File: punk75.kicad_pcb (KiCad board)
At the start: 2 copper layers, 285.8 x 124.6 mm, 184 parts, among them J1 AVR-ISP-6, SW1 RESET, SW2 BOOT, U1 ATmega32A-PU, Y1 16MHz

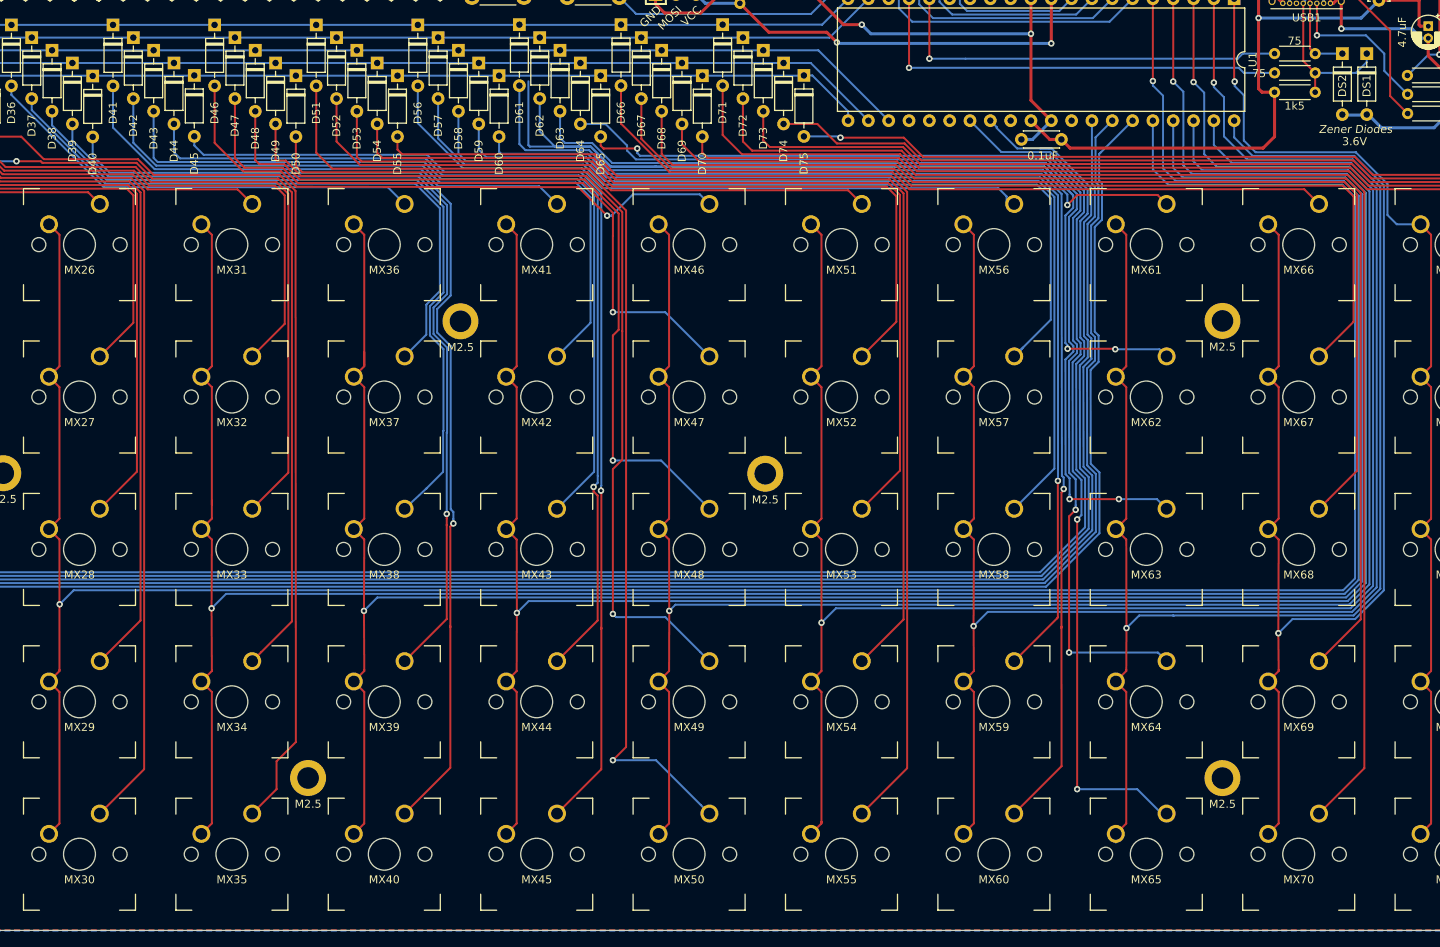
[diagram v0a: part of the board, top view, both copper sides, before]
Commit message: added extra switches to allow 2u in bottom row
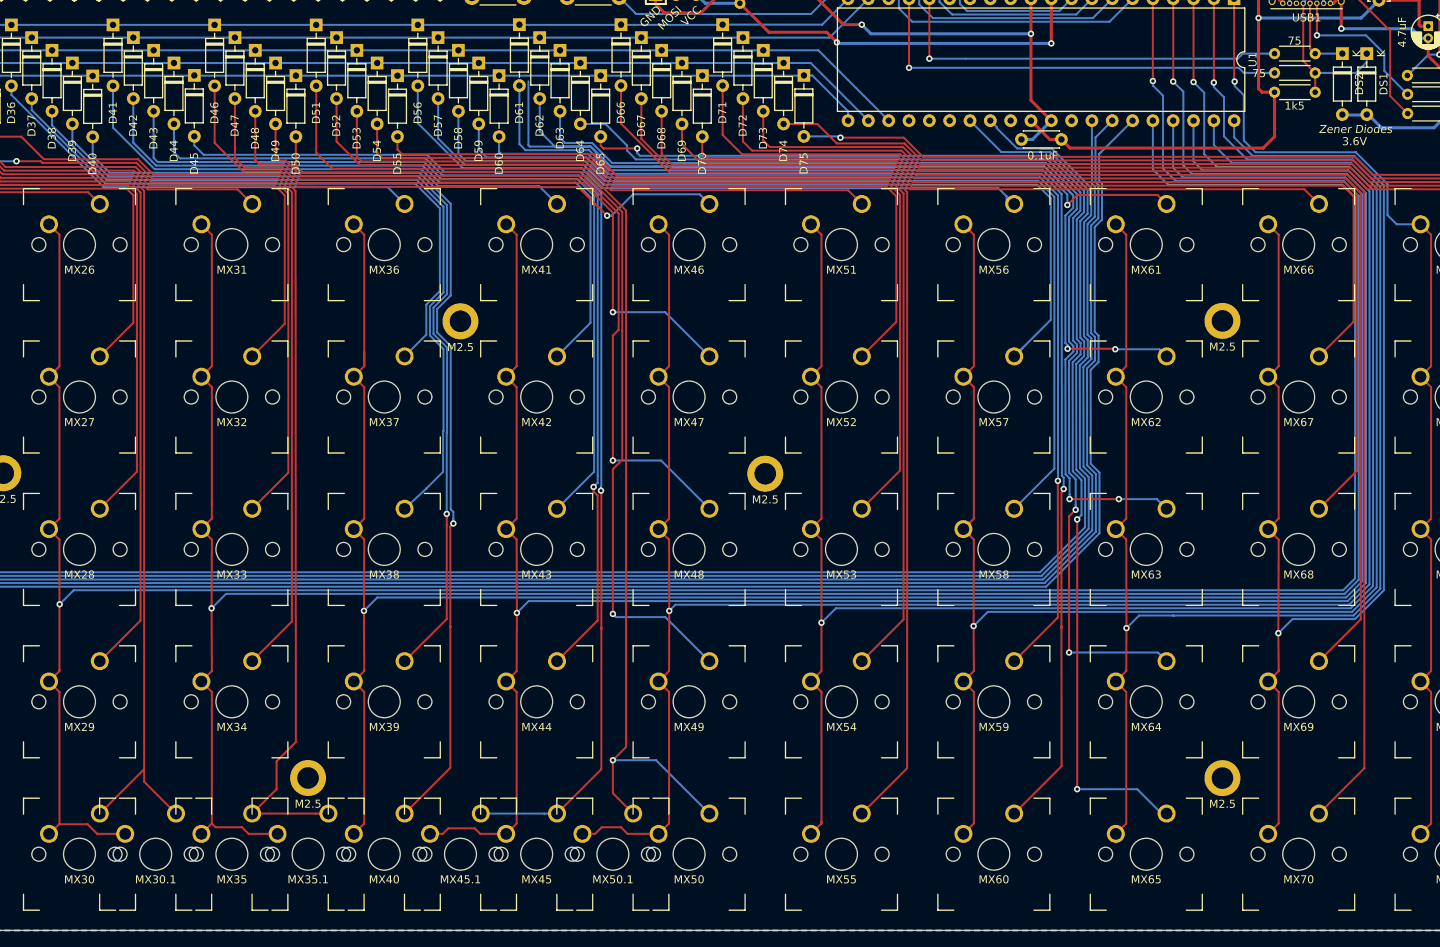
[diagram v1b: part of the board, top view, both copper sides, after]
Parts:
- added MX30.1: MX-NoLED, modded_footprints:MXOnly-1U-NoLED, F.Cu at (193.7, 220.7)
- added MX35.1: MX-NoLED, modded_footprints:MXOnly-1U-NoLED, F.Cu at (212.7, 220.7)
- added MX45.1: MX-NoLED, modded_footprints:MXOnly-1U-NoLED, F.Cu at (231.8, 220.7)
- added MX50.1: MX-NoLED, modded_footprints:MXOnly-1U-NoLED, F.Cu at (250.8, 220.7)
- DS1, DS2: footprint modded_footprints:D_DO-35_SOD27_P7.62mm_Horizontal -> Diode_THT:D_DO-35_SOD27_P7.62mm_Horizontal
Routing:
- net COL9: track 247.2 -> 257.4 mm
- net COL8: track 282.6 -> 292.7 mm
- net Net-(D35-Pad2): track 121.0 -> 130.5 mm
- net Net-(D45-Pad2): track 135.1 -> 144.1 mm
- net COL5: track 324.3 -> 333.0 mm
- net COL6: track 321.5 -> 330.2 mm
- net Net-(D50-Pad2): track 131.5 -> 139.2 mm
- net Net-(D30-Pad2): track 115.8 -> 123.0 mm

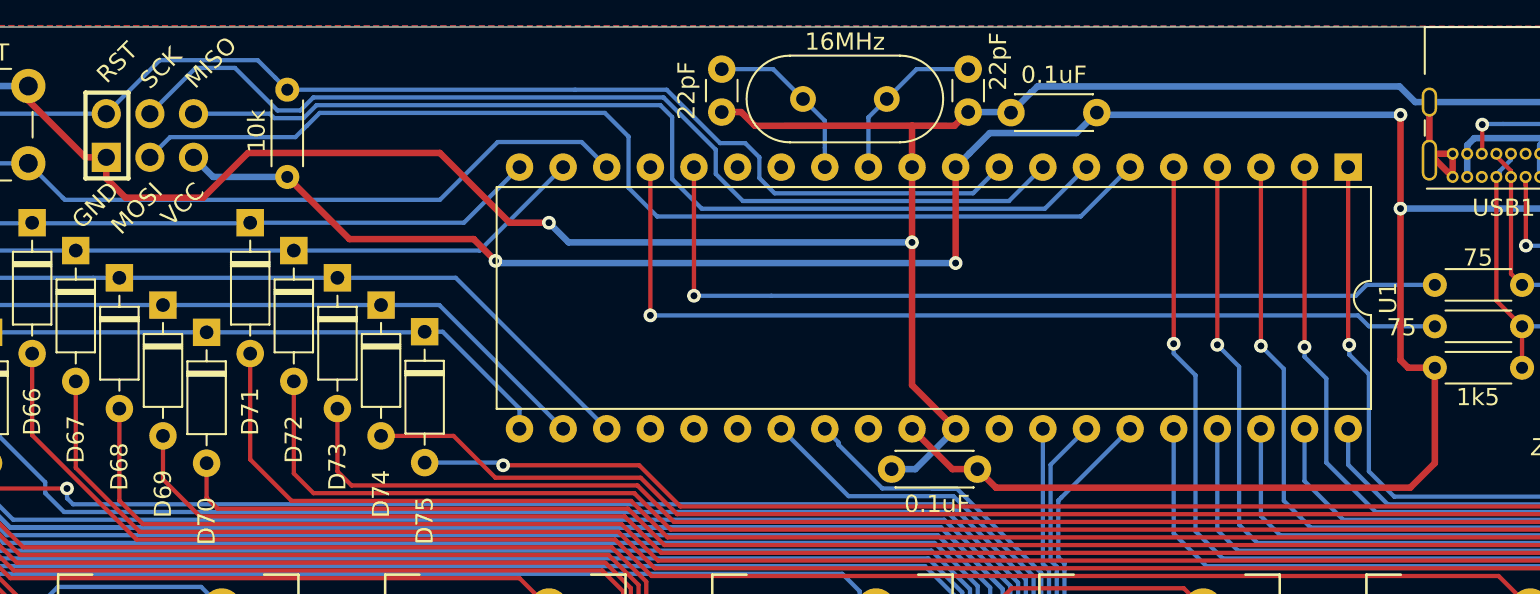
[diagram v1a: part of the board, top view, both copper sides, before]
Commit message: changed usb tracks using differential pair
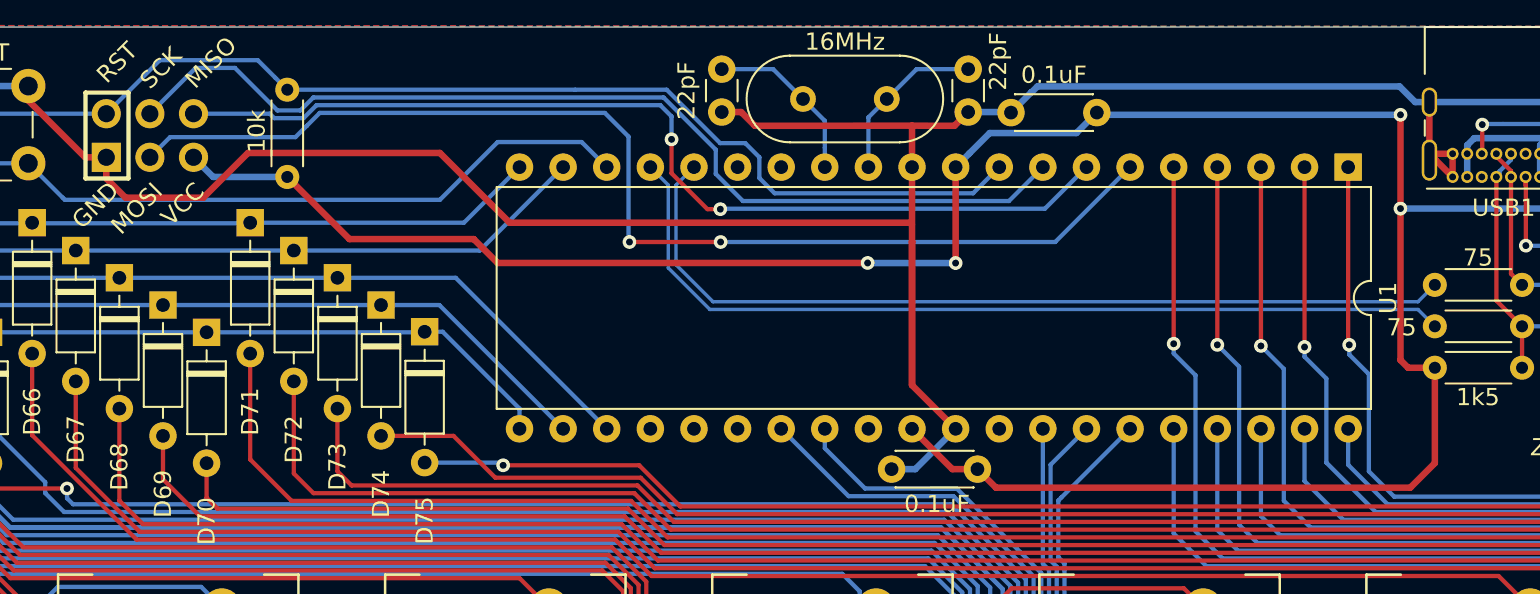
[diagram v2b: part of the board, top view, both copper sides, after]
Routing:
- net GND: track 208.8 -> 216.7 mm, vias 3 -> 1
- net MOSI: track 63.6 -> 66.6 mm, vias 0 -> 2
- net D-: track 55.1 -> 52.9 mm, vias 1 -> 0
- net D+: track 51.5 -> 52.2 mm, vias 1 -> 0
- net COL1: track 350.1 -> 350.7 mm
- net MISO: track 58.0 -> 57.9 mm, vias 0 -> 2

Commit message: added extra decoration
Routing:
- added copper zone on B.Cu, net (none)
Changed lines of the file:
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@@
     (36 B.SilkS user)
     (37 F.SilkS user)
-    (38 B.Mask user hide)
-    (39 F.Mask user hide)
+    (38 B.Mask user)
+    (39 F.Mask user)
     (40 Dwgs.User user hide)
     (41 Cmts.User user hide)
@@
       )
     )
+  )
+  (zone (net 0) (net_name "") (layer B.Cu) (hatch edge 0.508)
+    (connect_pads (clearance 0.508))
+    (min_thickness 0.254)
+    (fill yes (arc_segments 32) (thermal_gap 0.508) (thermal_bridge_width 0.508))
+    (polygon
+      (pts
+        (xy 334.01 165.862) (xy 331.47 170.307) (xy 326.263 170.307) (xy 323.723 165.862) (xy 326.263 161.29)
+        (xy 331.47 161.29)
+      )
+    )
+  )
+  (zone (net 0) (net_name "") (layer B.Cu) (hatch edge 0.508)
+    (connect_pads (clearance 0.508))
+    (min_thickness 0.254)
+    (fill yes (arc_segments 32) (thermal_gap 0.508) (thermal_bridge_width 0.508))
+    (polygon
+      (pts
+        (xy 325.501 170.688) (xy 322.961 175.26) (xy 317.754 175.26) (xy 315.087 170.688) (xy 317.754 166.243)
+        (xy 322.961 166.243)
+      )
+    )
+  )
+  (zone (net 0) (net_name "") (layer B.Cu) (hatch edge 0.508)
+    (connect_pads (clearance 0.508))
+    (min_thickness 0.254)
+    (fill yes (arc_segments 32) (thermal_gap 0.508) (thermal_bridge_width 0.508))
+    (polygon
+      (pts
+        (xy 334.01 175.768) (xy 331.47 180.213) (xy 326.263 180.213) (xy 323.596 175.768) (xy 326.263 171.196)
+        (xy 331.47 171.196)
+      )
+    )

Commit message: changed footprints to my modded MX-Alps hybrids
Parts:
- MX1, MX10, MX11, MX12, MX13, MX14, MX15, MX16, MX17, MX18, MX19, MX2, MX20, MX21, MX22, MX23, MX24, MX25, MX26, MX27, MX28, MX29, MX3, MX30, MX31, MX32, MX33, MX34, MX35, MX36, MX37, MX38, MX39, MX4, MX40, MX41, MX42, MX43, MX44, MX45, MX46, MX47, MX48, MX49, MX5, MX50, MX51, MX52, MX53, MX54, MX55, MX56, MX57, MX58, MX59, MX6, MX60, MX61, MX62, MX63, MX64, MX65, MX66, MX67, MX68, MX69, MX7, MX70, MX71, MX72, MX73, MX74, MX75, MX8, MX9: footprint modded_footprints:MXOnly-1U-NoLED -> MX_Alps_Hybrid:MX-1U-NoLED
- MX30.1, MX35.1, MX45.1, MX50.1: footprint modded_footprints:MXOnly-1U-NoLED -> MX_Alps_Hybrid:MX-2U-NoLED
- turned MX30.1 to 180 degrees
- turned MX35.1 to 180 degrees
- turned MX45.1 to 180 degrees
- turned MX50.1 to 180 degrees
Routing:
- net COL6: track 330.2 -> 345.6 mm
- net COL5: track 333.0 -> 346.2 mm
- net Net-(D30-Pad2): track 123.0 -> 135.1 mm, vias 0 -> 1
- net Net-(D45-Pad2): track 144.1 -> 153.8 mm
- net COL8: track 292.7 -> 301.2 mm
- net Net-(D50-Pad2): track 139.2 -> 147.7 mm
- net Net-(D35-Pad2): track 130.5 -> 137.8 mm
- net COL7: track 287.7 -> 292.4 mm
- net Net-(D40-Pad2): track 130.0 -> 131.8 mm
- net COL9: track 257.4 -> 256.6 mm

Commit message: added configurable led and rewired all colums to new ports
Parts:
- added LED2: LED2, LED_THT:LED_D3.0mm, F.Cu at (351.9, 111.5)
- added R8: 1k5, Resistor_THT:R_Axial_DIN0204_L3.6mm_D1.6mm_P5.08mm_Horizontal, F.Cu at (350.1, 121.2)
- moved LED1 2.86 mm to (357.0, 111.5)
- moved C5 0.95 mm to (352.7, 116.2)
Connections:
- U1 pad 1: COL14 -> Net-(U1-Pad1)
- U1 pad 15: Net-(U1-Pad15) -> LED2
- U1 pad 2: COL12 -> Net-(U1-Pad2)
- U1 pad 24: Net-(U1-Pad24) -> COL0
- U1 pad 25: Net-(U1-Pad25) -> COL1
- U1 pad 26: Net-(U1-Pad26) -> COL4
- U1 pad 27: COL0 -> COL3
- U1 pad 28: COL1 -> COL2
- U1 pad 3: COL10 -> COL13
- U1 pad 33: COL2 -> COL5
- U1 pad 34: COL3 -> COL6
- U1 pad 35: COL4 -> COL7
- U1 pad 36: COL5 -> COL8
- U1 pad 37: COL7 -> COL10
- U1 pad 38: COL9 -> COL12
- U1 pad 39: COL11 -> COL14
- U1 pad 4: COL8 -> COL11
- U1 pad 40: COL13 -> Net-(U1-Pad40)
- U1 pad 5: COL6 -> COL9
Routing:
- net LED2: track 0.00 -> 64.3 mm, vias 0 -> 4
- net COL13: track 169.9 -> 190.8 mm, vias 1 -> 2
- net COL4: track 288.1 -> 308.5 mm
- net COL11: track 208.4 -> 228.0 mm, vias 1 -> 2
- net COL9: track 256.6 -> 274.3 mm, vias 1 -> 2
- net COL3: track 305.5 -> 321.7 mm
- net COL8: track 301.2 -> 286.6 mm, vias 2 -> 1
- net COL10: track 244.2 -> 230.9 mm, vias 2 -> 1
- net COL6: track 345.6 -> 332.7 mm, vias 2 -> 1
- net COL2: track 322.9 -> 335.1 mm
- net COL14: track 127.6 -> 116.2 mm, vias 1 -> 0
- net COL12: track 205.6 -> 194.7 mm, vias 2 -> 1
- net Net-(LED2-Pad1): track 0.00 -> 10.4 mm
- net COL0: track 369.2 -> 376.8 mm
- net GND: track 216.7 -> 209.2 mm
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
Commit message: added 2 rotary encoders and changed some traces to use them
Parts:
- added RE1: Rotary_Encoder_Switch, Rotary_Encoder:RotaryEncoder_Alps_EC11E-Switch_Vertical_H20mm_CircularMountingHoles, F.Cu at (86.4, 152.0)
- added RE2: Rotary_Encoder_Switch, Rotary_Encoder:RotaryEncoder_Alps_EC11E-Switch_Vertical_H20mm_CircularMountingHoles, F.Cu at (353.2, 152.0)
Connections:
- net Net-(D1-Pad2) renamed ROW_SWITCH1
- net Net-(D71-Pad2) renamed ROW_SWITCH2
- U1 pad 1: Net-(U1-Pad1) -> R2B
- U1 pad 14: Net-(U1-Pad14) -> R1A
- U1 pad 15: LED2 -> R1B
- U1 pad 2: Net-(U1-Pad2) -> R2A
- U1 pad 40: Net-(U1-Pad40) -> LED2
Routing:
- net R1A: track 0.00 -> 267.5 mm, vias 0 -> 1
- net R1B: track 0.00 -> 262.0 mm, vias 0 -> 1
- net R2A: track 0.00 -> 71.7 mm, vias 0 -> 1
- net R2B: track 0.00 -> 67.4 mm, vias 0 -> 1
- net LED2: track 64.3 -> 37.1 mm, vias 4 -> 2
- net COL14: track 116.2 -> 127.8 mm
- net COL0: track 376.8 -> 383.4 mm
- net Net-(D73-Pad2): track 140.9 -> 145.0 mm
- net Net-(D72-Pad2): track 125.3 -> 129.4 mm
- net ROW_SWITCH2: track 103.3 -> 106.1 mm
- net ROW_SWITCH1: track 20.2 -> 22.4 mm
- net Net-(D74-Pad2): track 155.4 -> 157.0 mm
- net Net-(D75-Pad2): track 172.1 -> 173.5 mm
- net Net-(D4-Pad2): track 70.0 -> 71.4 mm
- net Net-(D2-Pad2): track 38.0 -> 39.1 mm
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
